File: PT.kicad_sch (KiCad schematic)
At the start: 4 parts

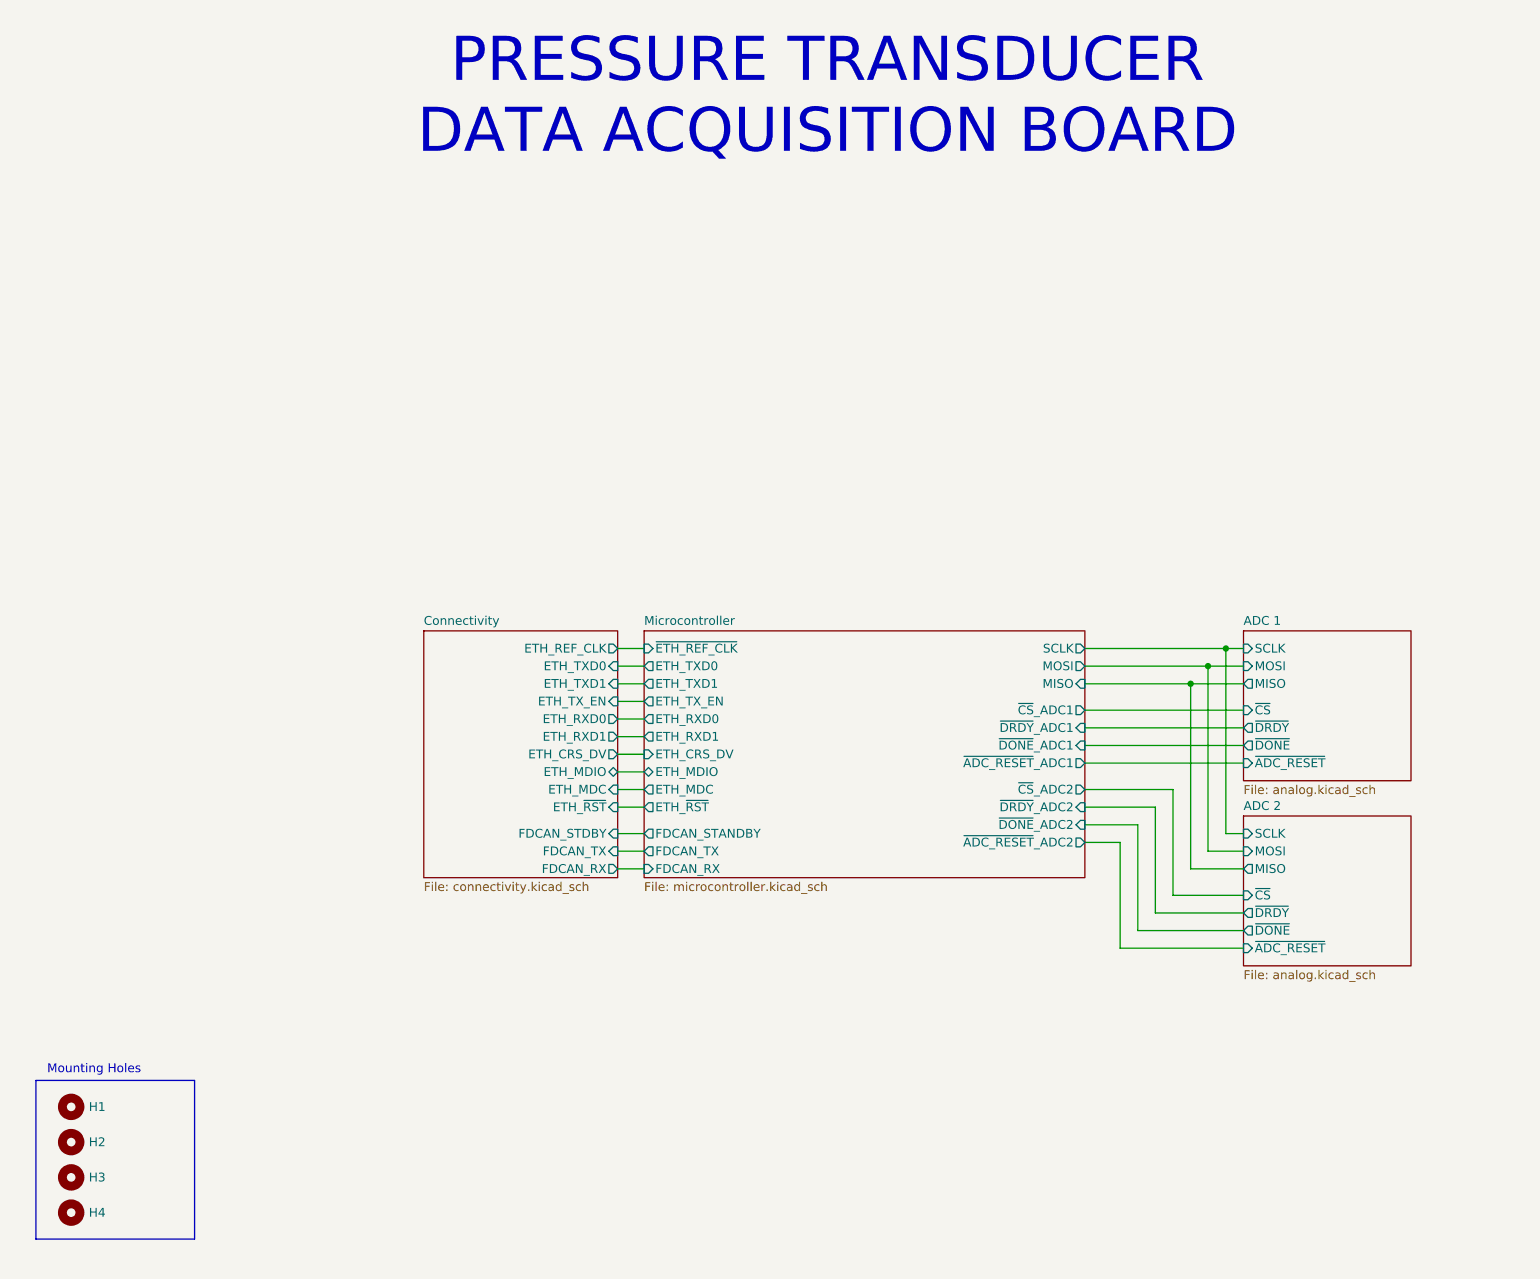
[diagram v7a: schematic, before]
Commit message: New layout just dropped (need to change silkscreen on USB and update PT.ioc)
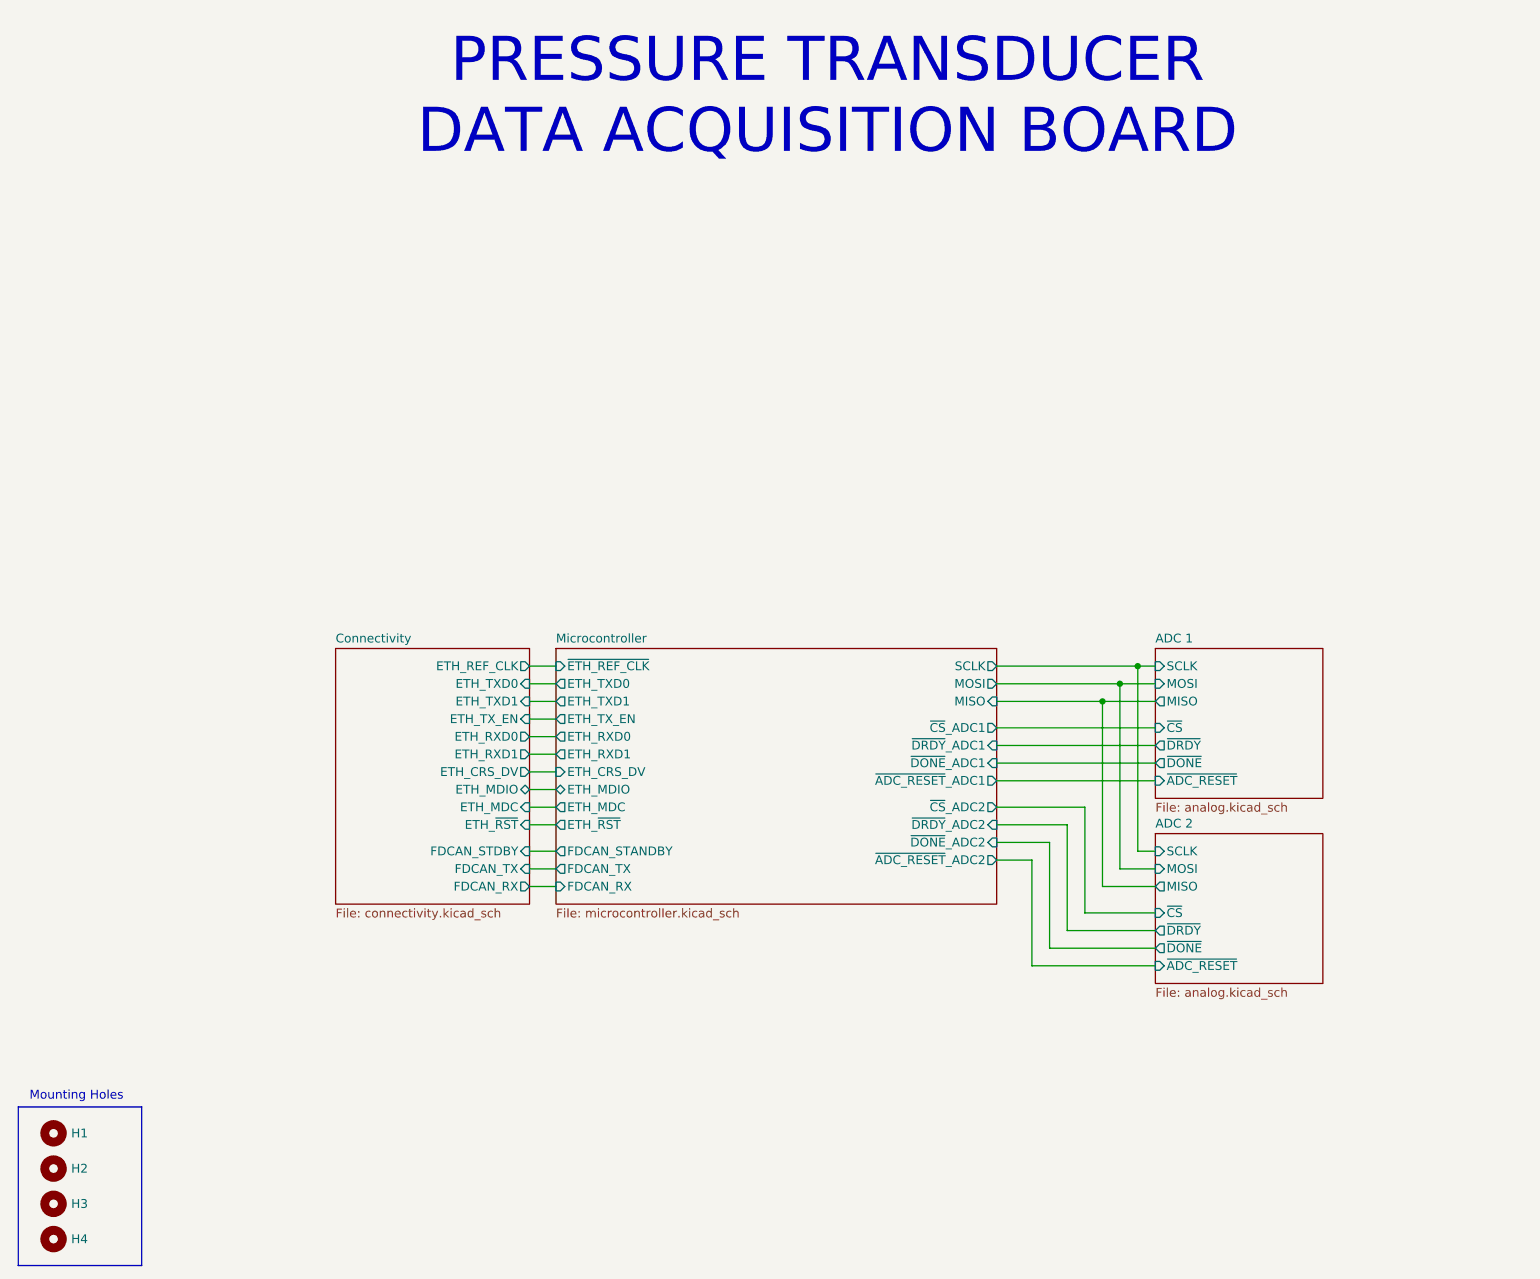
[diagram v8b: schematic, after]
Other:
- moved on the sheet: H1, H2, H3, H4
